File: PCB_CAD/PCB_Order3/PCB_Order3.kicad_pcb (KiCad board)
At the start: 4 copper layers, 164.4 x 127.2 mm, 93 parts, among them J1 Conn_01x03_Socket, SW1 SLW-883935-2A-D

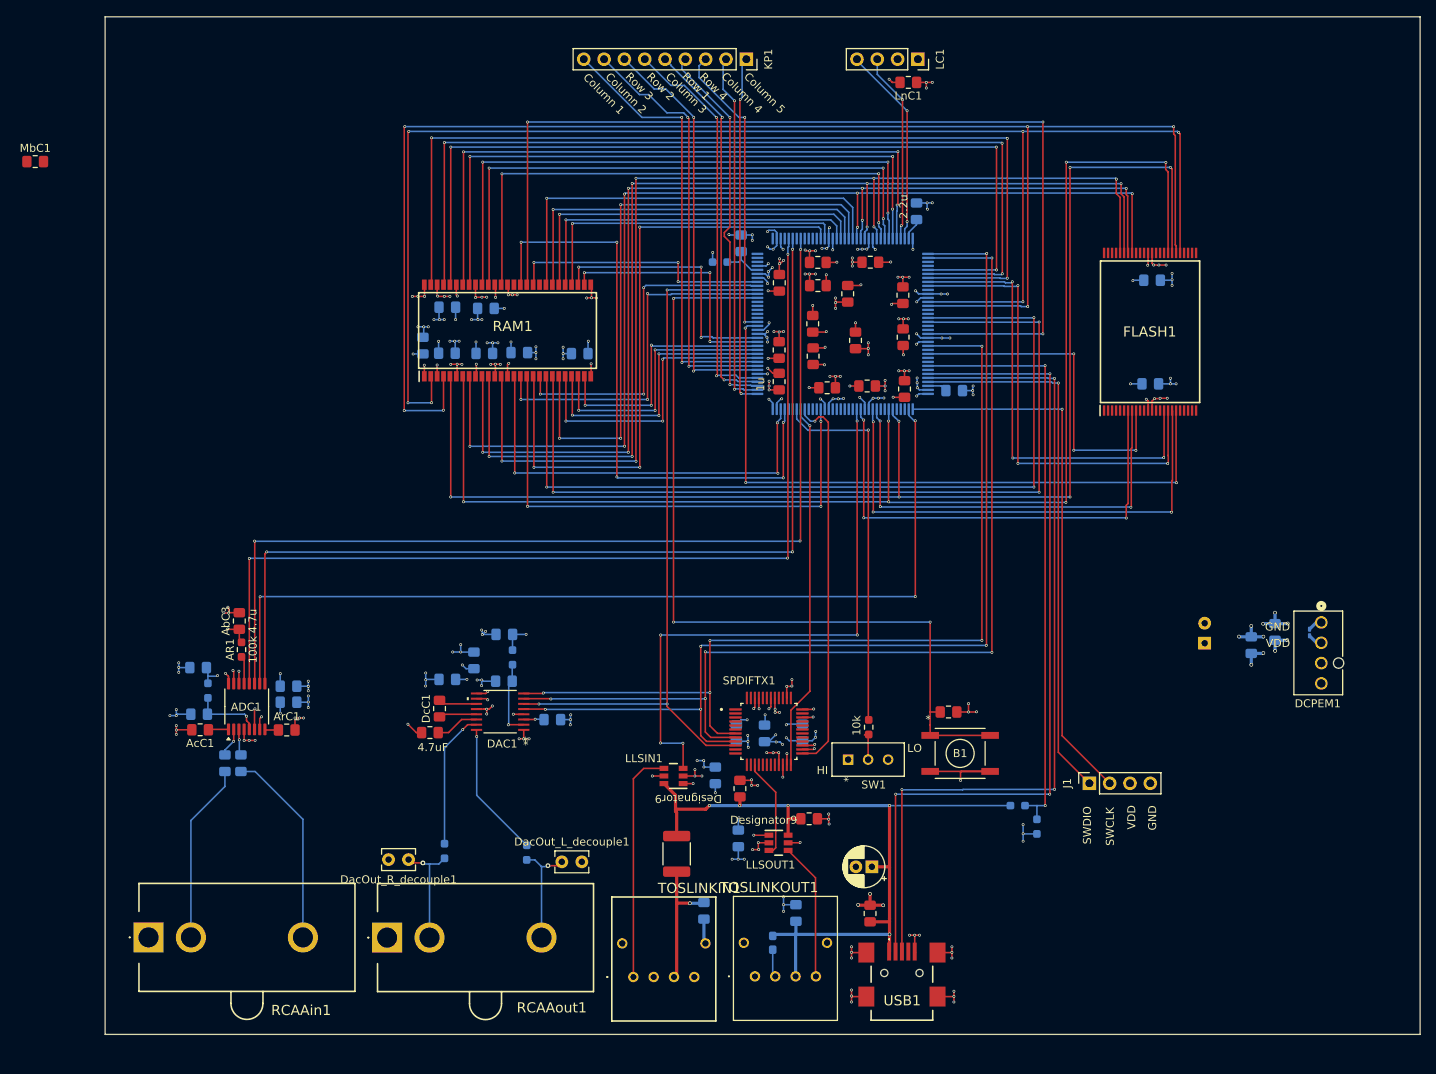
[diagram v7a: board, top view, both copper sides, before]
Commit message: Main board final review complete and Gerbers generated. This board would cost 40 bucks extra at JLC because of the 20/35 vias, preferentially needs updated to minimally 30/45 vias if we do not want to pay that. For further work on this board git add .git add .DO NOTgit add .git add . 'update PCB from schematic,' I introduced a lot of breaking differences due to being lazy.
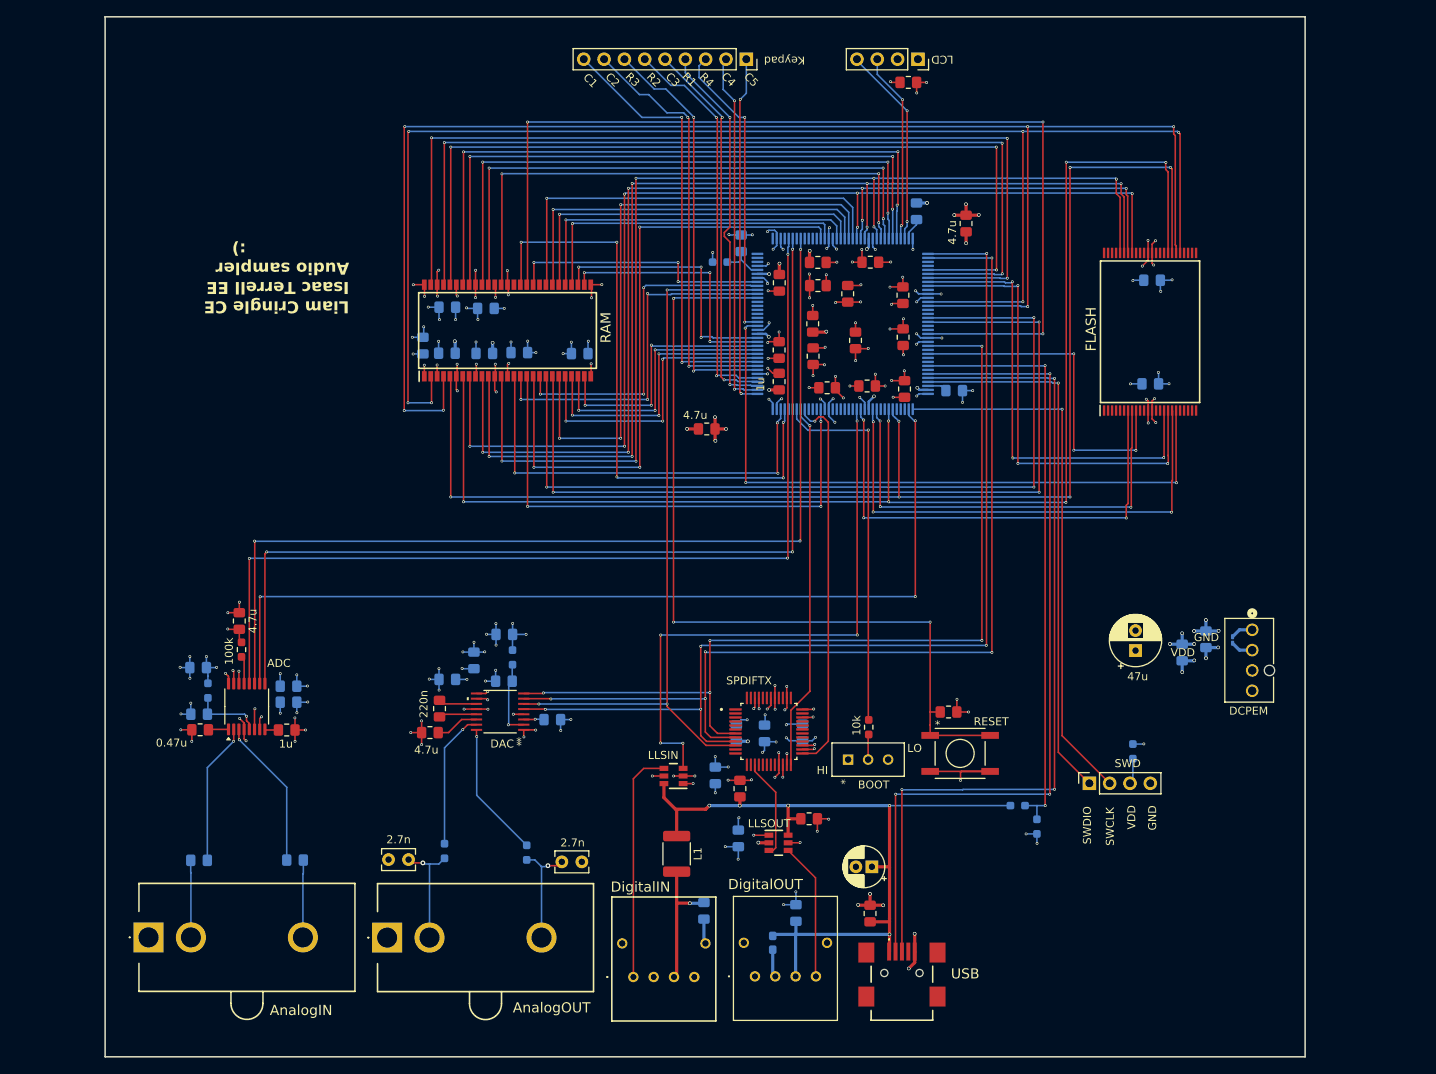
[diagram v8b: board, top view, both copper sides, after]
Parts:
- added MbC2: 4.7u, Capacitor_SMD:C_0805_2012Metric_Pad1.18x1.45mm_HandSolder, F.Cu at (135.4, 71.0)
- added SWDRes: 10k, Resistor_SMD:R_0603_1608Metric_Pad0.98x0.95mm_HandSolder, B.Cu at (156.3, 137.0)
- DacOut_L_res1, DacOut_R_res1: value 500 -> 510
- DcC1: value 220nF -> 220n
- DcC2: value 4.7uF -> 4.7u
- DrC1: value 2.2uF -> 2.2u
- PEC1: value 0.1u -> 1u
- PEC3: moved to F.Cu
- moved MbC1 90.4 mm to (103.0, 96.7)
- moved AdbC2 13.9 mm to (51.5, 150.6), turned to 180 degrees
- moved AdbC1 12.6 mm to (39.5, 150.6), turned to 0 degrees
- moved TVS1 9.66 mm to (168.7, 123.0)
- moved PEC3 8.69 mm to (156.6, 124.4)
- moved DCPEM 8.69 mm to (171.2, 121.8)
- moved PEC1 8.69 mm to (162.4, 124.6)
- moved PEC2 8.69 mm to (165.4, 123.0)
- renumbered ADC1 to ADC, RCAAin1 to AnalogIN, RCAAout1 to AnalogOUT, SW1 to BOOT, DAC1 to DAC, DCPEM1 to DCPEM, TOSLINKIN1 to DigitalIN, TOSLINKOUT1 to DigitalOUT, FLASH1 to FLASH, KP1 to Keypad, TOSLINKL1 to L1, LC1 to LCD, LLSIN1 to LLSIN, LLSOUT1 to LLSOUT, uController1 to Microcontroller, RAM1 to RAM, B1 to RESET, SPDIFTX1 to SPDIFTX, J1 to SWD, USB1 to USB
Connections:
- SWD pad 3: VDD -> SWDVDD
- USB pad 6: GNDD -> unconnected-USBMP1
- USB pad 7: GNDD -> unconnected-USBMP2
- USB pad 8: GNDD -> unconnected-USBMP3
- USB pad 9: GNDD -> unconnected-USBMP4
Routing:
- net Net-(ADC1-LIN): track 3.29 -> 18.8 mm
- net Net-(AdbC2-Pad1): track 25.0 -> 9.69 mm
- net Net-(ADC1-RIN): track 3.65 -> 17.7 mm
- net Net-(AdbC1-Pad1): track 22.5 -> 9.64 mm
- net GNDD: track 289.9 -> 278.2 mm, vias 262 -> 175
- net VDD: track 123.8 -> 135.0 mm, vias 78 -> 85
- net SWDVDD: track 0.00 -> 3.23 mm
- net Net-(SR1-Pad1): track 3.72 -> 3.17 mm
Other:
- board size 164.4 x 127.2 mm -> 150 x 130 mm
- board text added: "C1"
- board text added: "C2"
- board text added: "C3"
- board text added: "C4"
- board text added: "C5"
- board text added: "Liam Cringle CE Isaac Terrell EE Audio sampler :)"
- board text added: "R1"
- board text added: "R2"
- board text added: "R3"
- board text added: "R4"
- board text added: "With thanks to Jesus Christ and Andrew Sheaff"
- board text removed: "2.2u"
- board text removed: "Column 1"
- board text removed: "Column 2"
- board text removed: "Column 3"
- board text removed: "Column 4"
- board text removed: "Column 5"
- board text removed: "Row 1"
- board text removed: "Row 2"
- board text removed: "Row 3"
- board text removed: "Row 4"
